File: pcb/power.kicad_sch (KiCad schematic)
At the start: 53 parts, among them Q1 NFET_250V_10A_TPH1110FNH,L1Q, U5 REG_SW_BOOST_TI_TLV61046ADBV, U6 REG_SW_BOOST_TI_LM51561HPWPR, U7 REG_LDO_3V3_250mA_TI_LP5907MF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

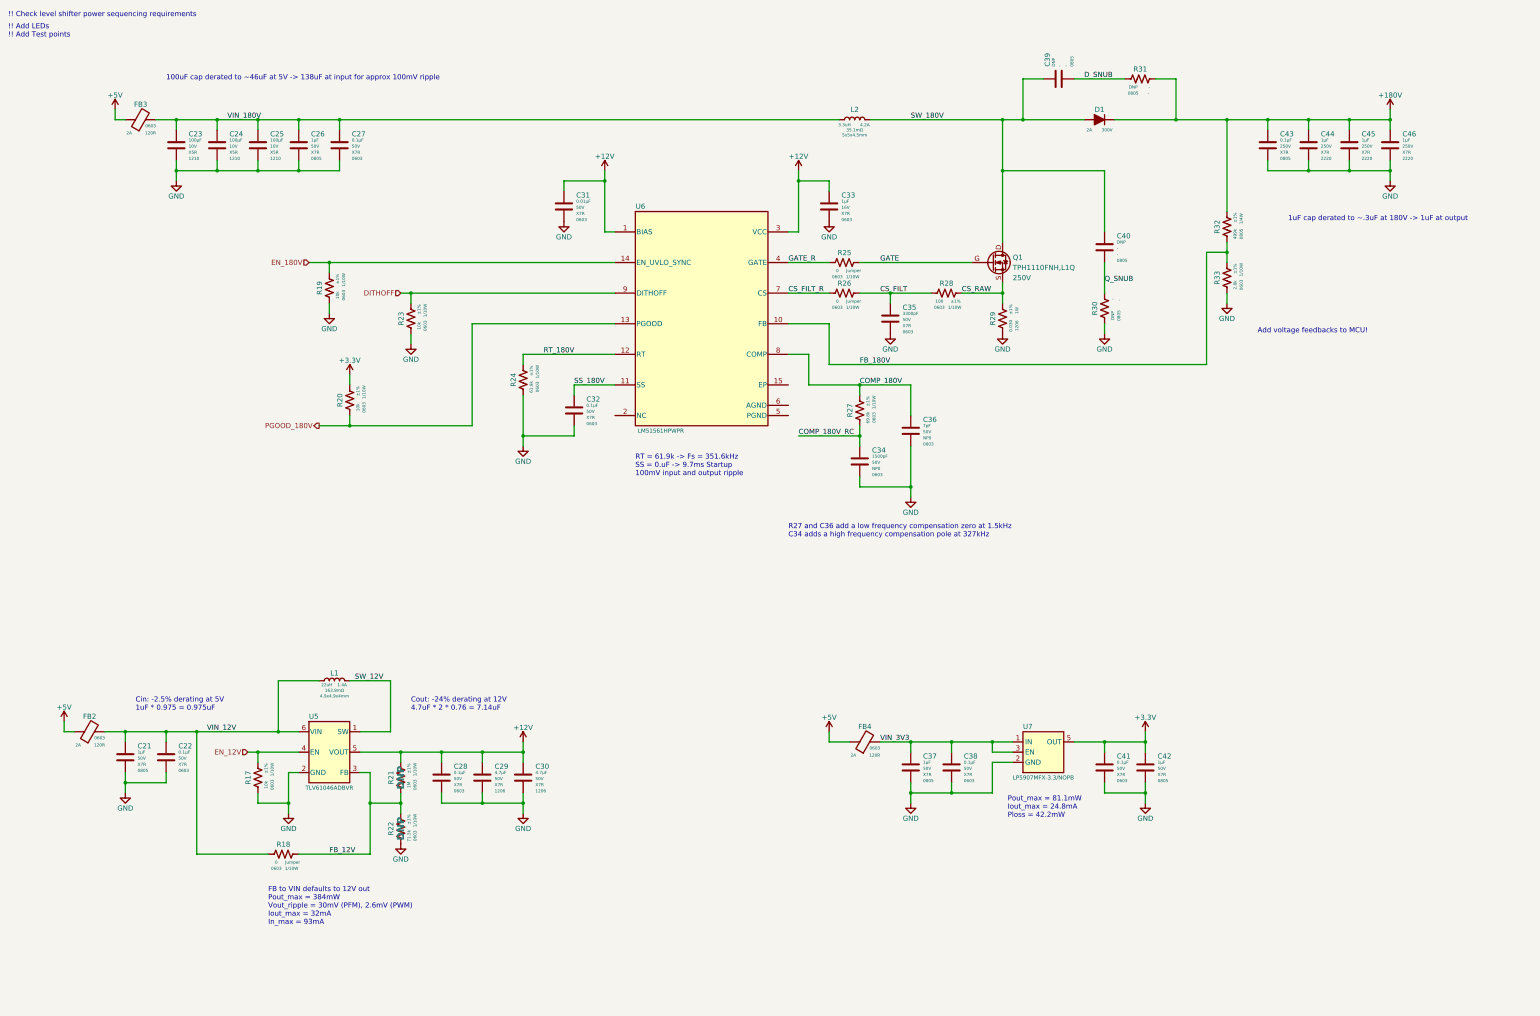
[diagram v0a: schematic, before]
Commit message: Added 12V and 180V sense lines
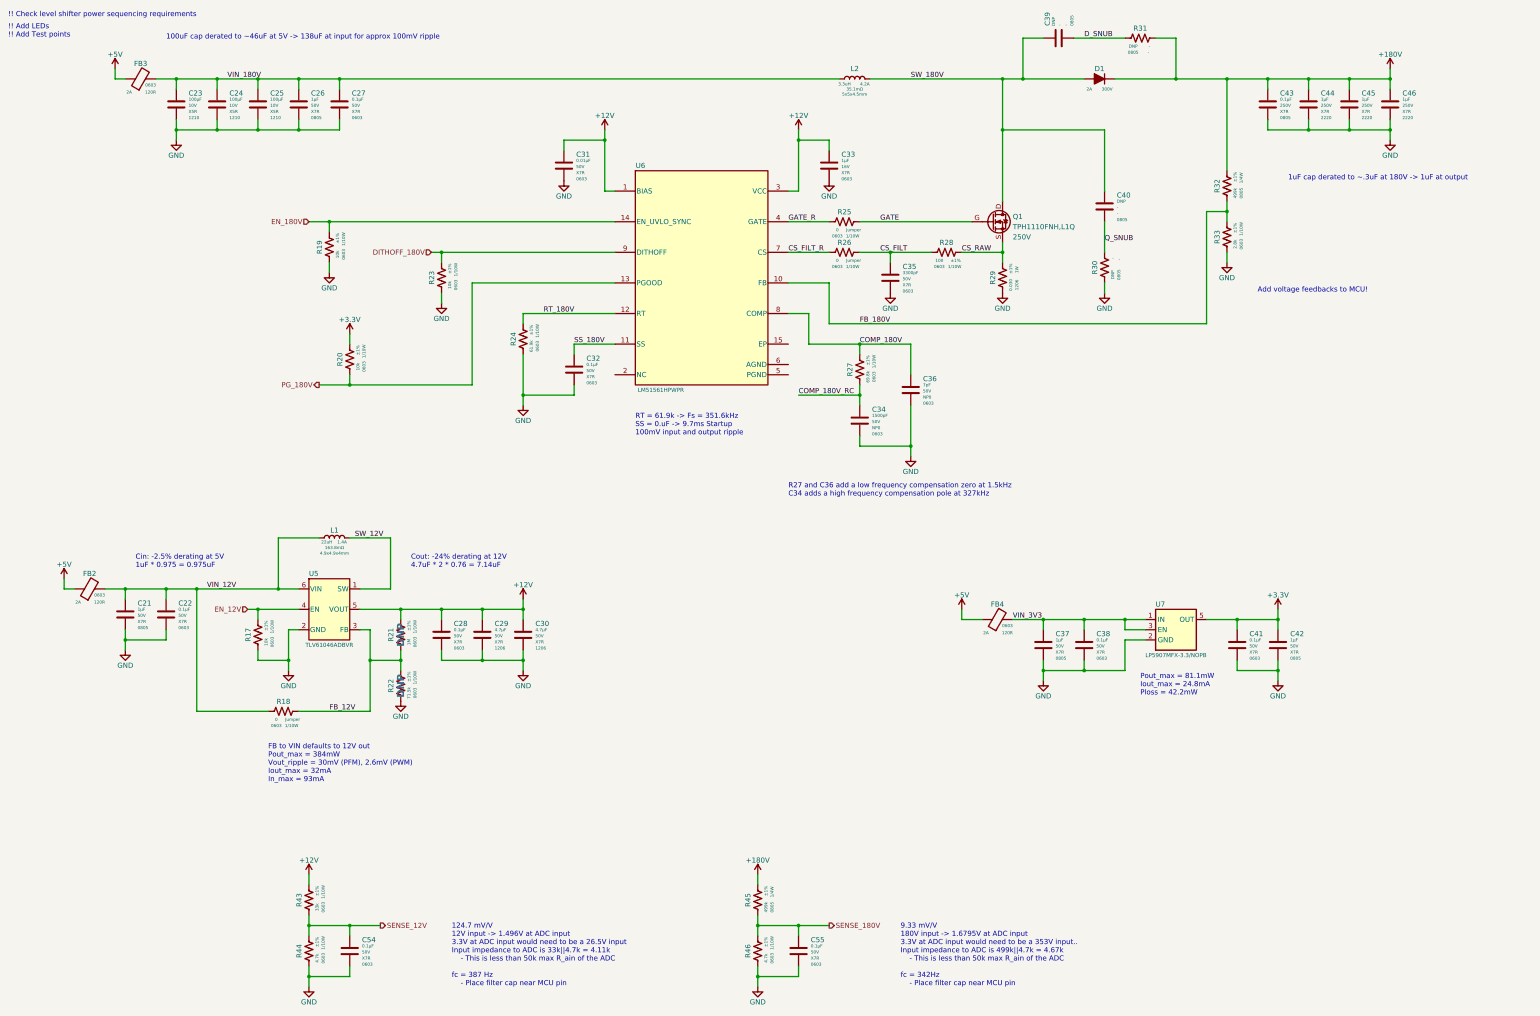
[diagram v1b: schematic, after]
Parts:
- added C54, C55: CAP_CER_0u1_50V_X7R_0603, Capacitor_SMD:C_0603_1608Metric, symbol .arjun:CAP_CER_0u1_50V_X7R_0603
- added R43: RES_33K_1P_1/10W_0603, Resistor_SMD:R_0603_1608Metric, symbol .arjun:RES_33K_1P_1/10W_0603
- added R44, R46: RES_4K7_1P_1/10W_0603, Resistor_SMD:R_0603_1608Metric, symbol .arjun:RES_4K7_1P_1/10W_0603
- added R45: RES_499K_1P_1/4W_0805, Resistor_SMD:R_0805_2012Metric, symbol .arjun:RES_499K_1P_1/4W_0805
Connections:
- net +12V: now also R43.1
- net 180V: now also R45.1
- net GND: now also C54.2, C55.2, R44.2, R46.2
- net DITHOFF renamed DITHOFF_180V
- net PGOOD_180V renamed PG_180V
- new net SENSE_12V: C54.1, R43.2, R44.1
- new net SENSE_180V: C55.1, R45.2, R46.1
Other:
- note added: "124.7 mV/V 12V input -> 1.496V at ADC input 3.3V at ADC input would need to be a 26.5V input Input impedance to ADC is 33k||4.7k = 4.11k - This is less than 50k max R_ain of the ADC fc = 387 Hz - Place filter cap near MCU pin"
- note added: "9.33 mV/V 180V input -> 1.6795V at ADC input 3.3V at ADC input would need to be a 353V input.. Input impedance to ADC is 499k||4.7k = 4.67k - This is less than 50k max R_ain of the ADC fc = 342Hz - Place filter cap near MCU pin"
- moved on the sheet: C21, C22, C23, C24, C25, C26, C27, C28, C29, C30, C31, C32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

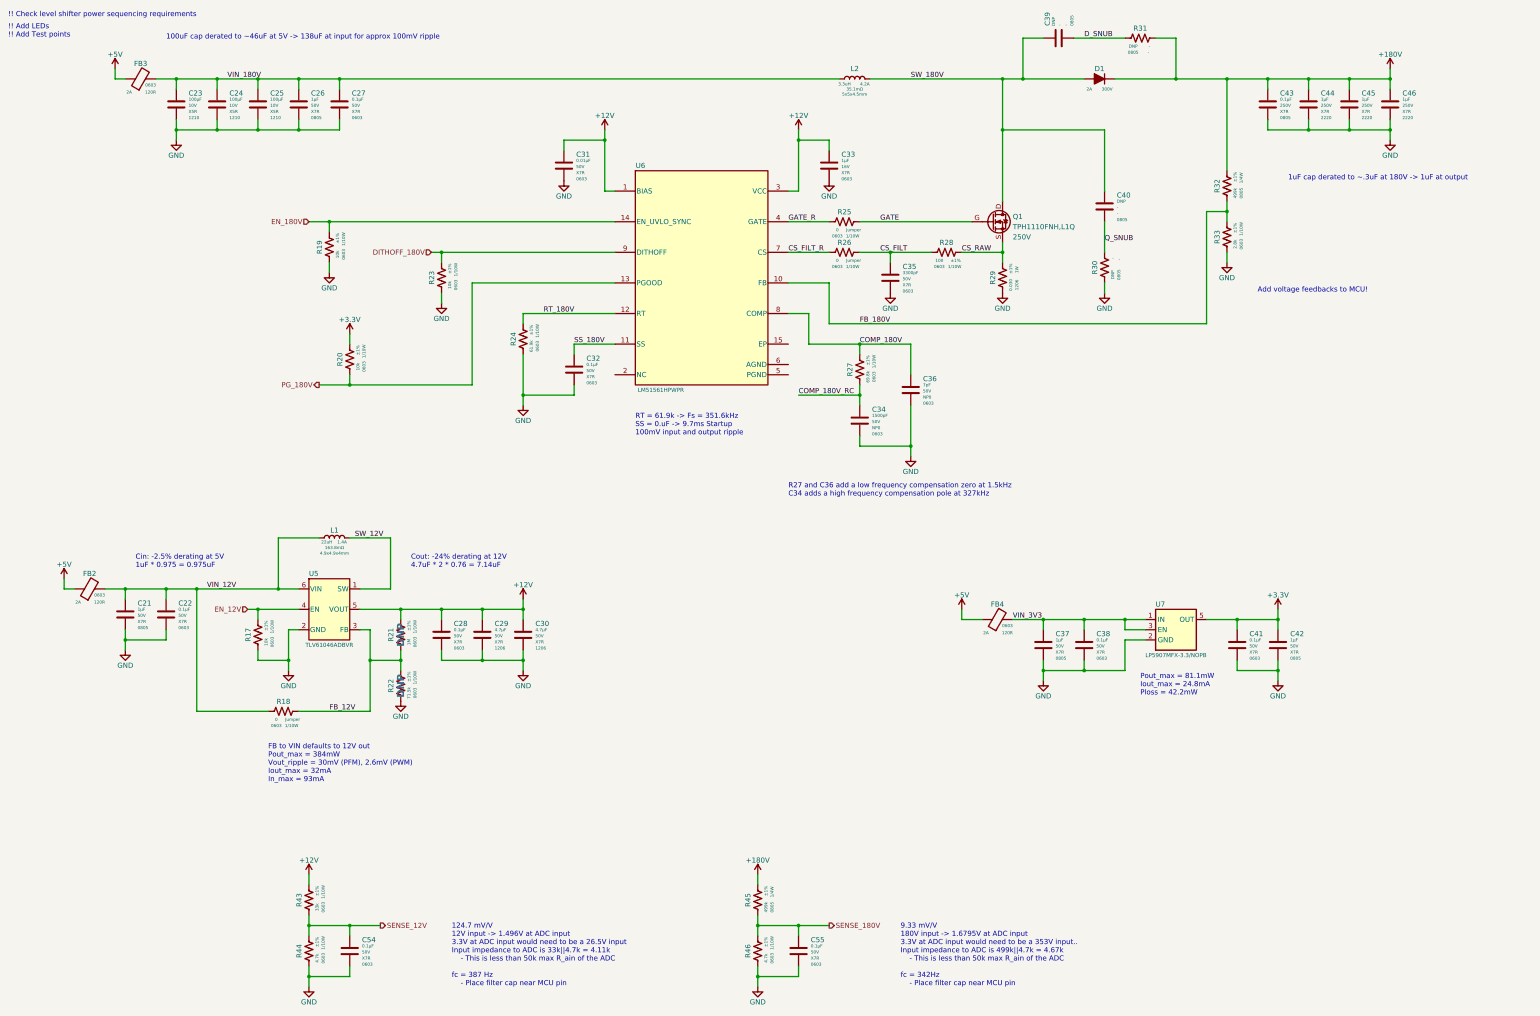
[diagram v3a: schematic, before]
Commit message: Added ESD protection to 5V input, leds, hw rev pins, and test points.
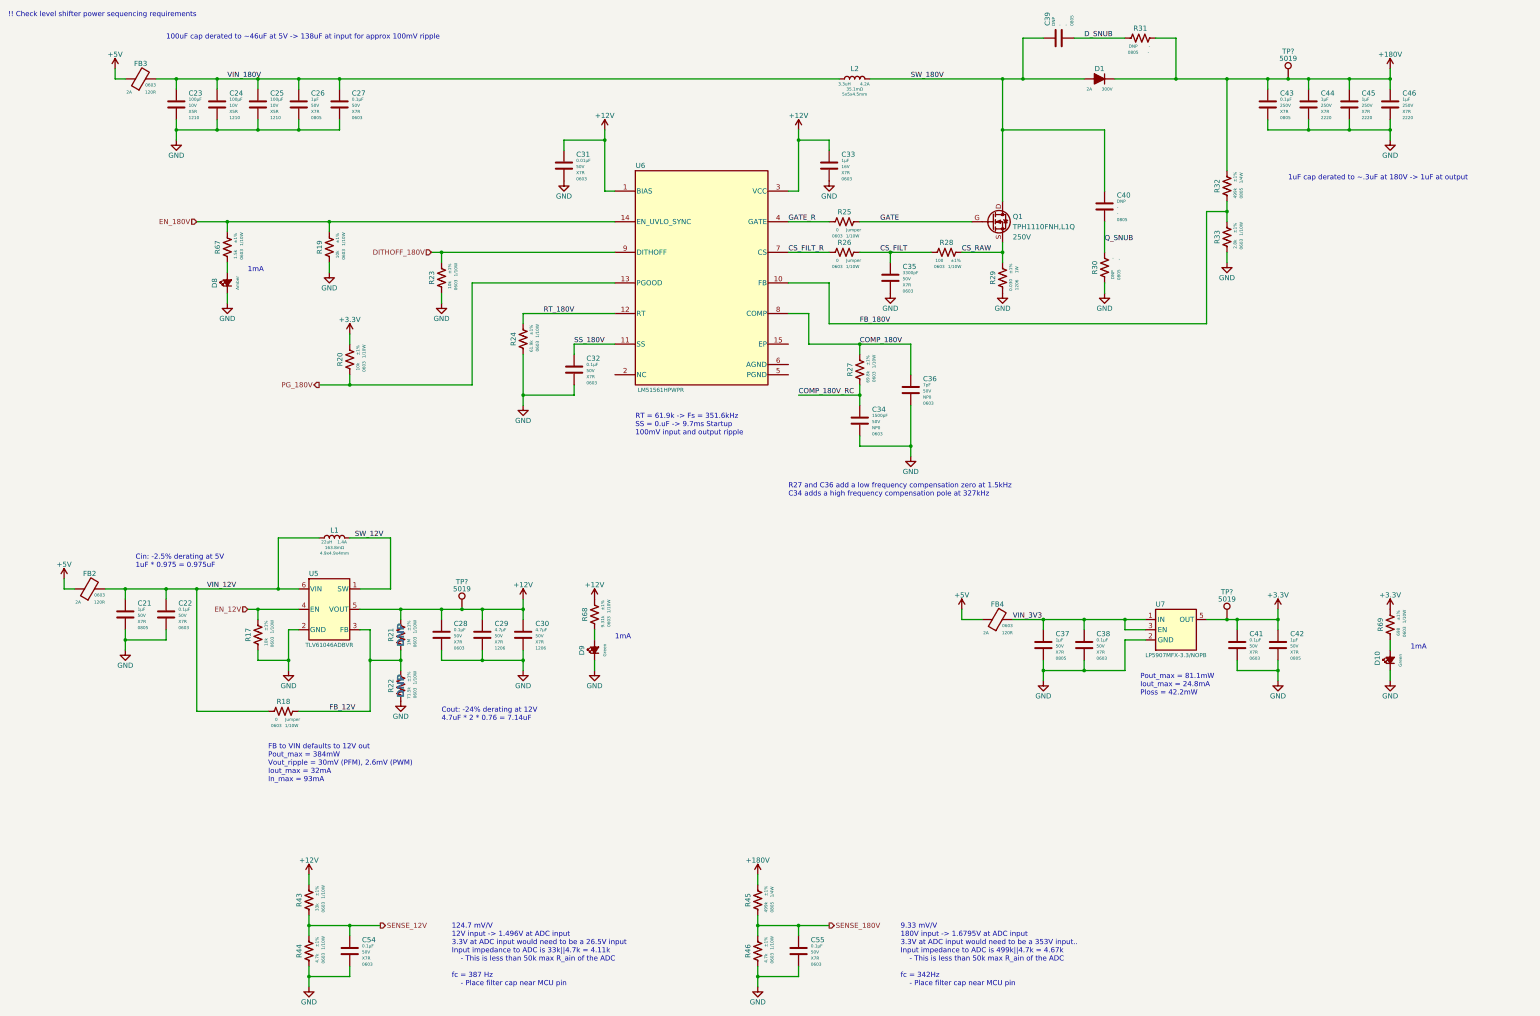
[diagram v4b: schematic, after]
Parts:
- added D10, D9: LED_GREEN_0603, LED_SMD:LED_0603_1608Metric, symbol .arjun:LED_GREEN_0603
- added D8: LED_AMBER_0603, LED_SMD:LED_0603_1608Metric, symbol .arjun:LED_AMBER_0603
- added R67: RES_1K5_1P_1/10W_0603, Resistor_SMD:R_0603_1608Metric, symbol .arjun:RES_1K5_1P_1/10W_0603
- added R68: RES_9K31_1P_1/10W_0603, Resistor_SMD:R_0603_1608Metric, symbol .arjun:RES_9K31_1P_1/10W_0603
- added R69: RES_698R_1P_1/10W_0603, Resistor_SMD:R_0603_1608Metric, symbol .arjun:RES_698R_1P_1/10W_0603
- added TP? (x3): TP_KEYSTONE_5019, arjun_footprints:TestPoint_Keystone_5019_Minature, symbol .arjun:TP_KEYSTONE_5019
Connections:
- net +12V: now also R68.1, TP?.1
- net +3.3V: now also R69.1, TP?.1
- net 180V: now also TP?.1
- net EN_180V: now also R67.1
- net GND: now also D10.1 (K), D8.1 (K), D9.1 (K)
- new net: D10.2 (A), R69.2
- new net: D9.2 (A), R68.2
- new net: D8.2 (A), R67.2
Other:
- note added: "1mA"
- note removed: "!! Add LEDs !! Add Test points"
- note removed: "Add voltage feedbacks to MCU!"
